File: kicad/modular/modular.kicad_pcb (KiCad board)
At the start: 2 copper layers, 50.5 x 78 mm, 53 parts, among them J1 CONN_PWR, J2 HEADER, J3 HEADER, U1 LM317, U2 LM337, U3 REF5010, U4 OPA4197

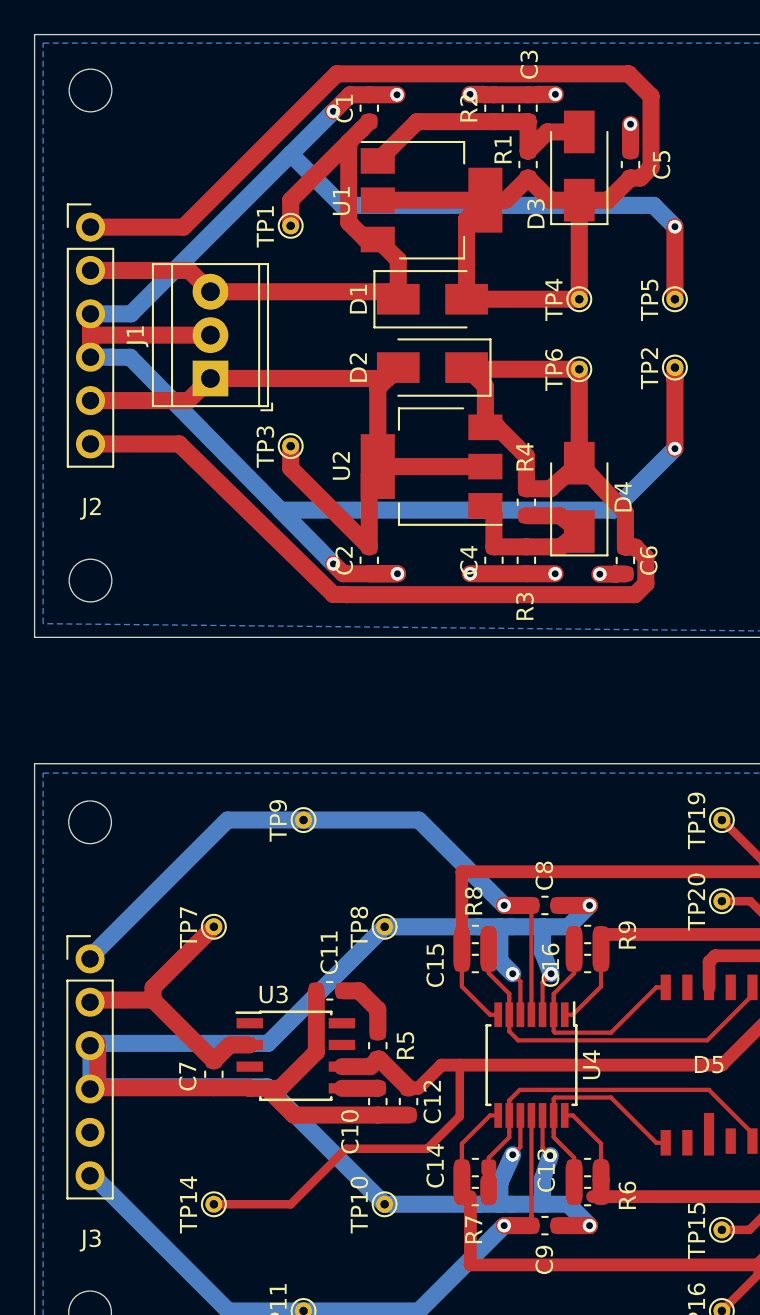
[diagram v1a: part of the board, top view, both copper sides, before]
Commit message: via stitched gnd trace of voltage reference, added zones around voltage regulators
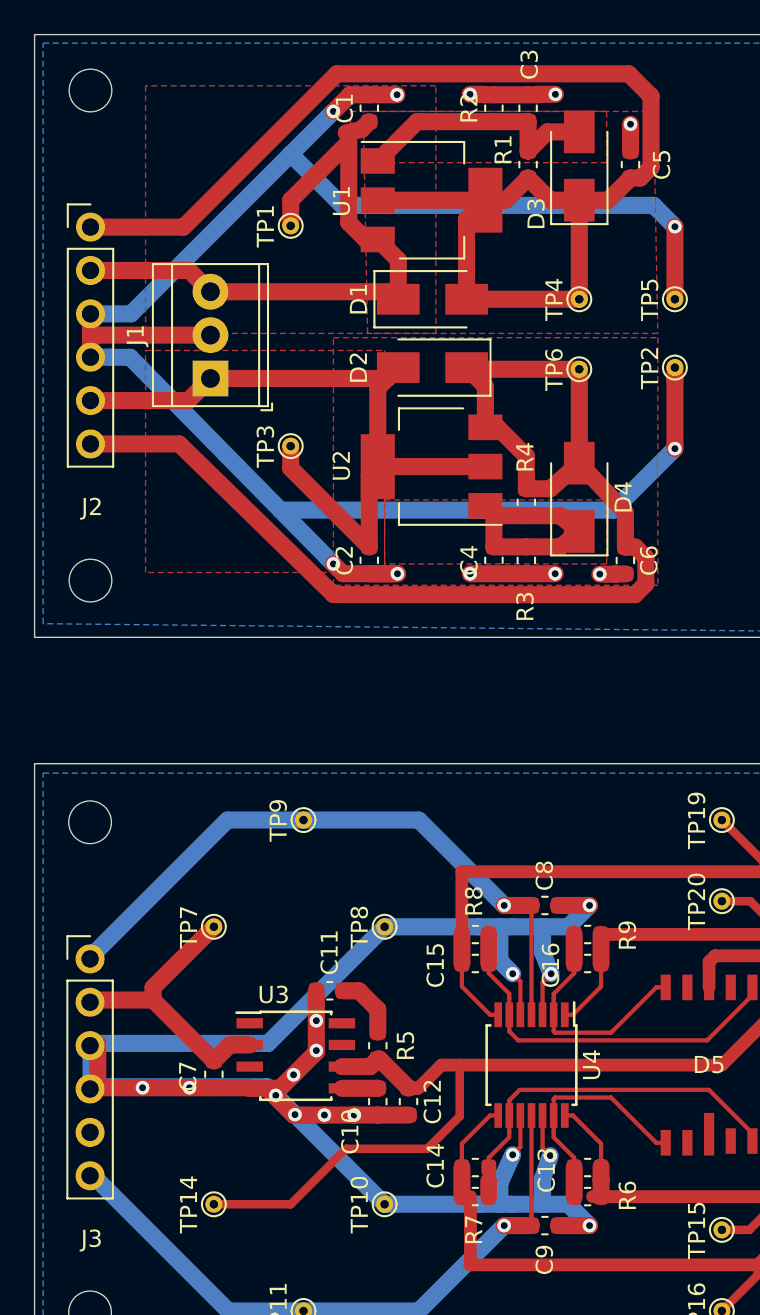
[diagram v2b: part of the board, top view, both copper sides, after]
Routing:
- net Net-(C4-Pad2): track 11.4 -> 14.0 mm
- net GND: vias 18 -> 27
- added copper zone on F.Cu, net +12V
- added copper zone on F.Cu, net +15V
- added copper zone on F.Cu, net -12V
- added copper zone on F.Cu, net -15V
- added copper zone on F.Cu, net Net-(C3-Pad1)
- added copper zone on F.Cu, net Net-(C4-Pad2)

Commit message: added pcb design of arithmetic board
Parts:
- added C17: 100n, Capacitor_SMD:C_0603_1608Metric, F.Cu at (205.7, 101.8)
- added C18: 100n, Capacitor_SMD:C_0603_1608Metric, F.Cu at (196.3, 98.5)
- added C19: 100n, Capacitor_SMD:C_0603_1608Metric, F.Cu at (193.4, 101.8)
- added C20: 100n, Capacitor_SMD:C_0603_1608Metric, F.Cu at (183.9, 98.5)
- added C21: ?, Capacitor_SMD:C_0603_1608Metric, F.Cu at (198.7, 94.4)
- added C22: ?, Capacitor_SMD:C_0603_1608Metric, F.Cu at (173.8, 94.5)
- added C23: ?, Capacitor_SMD:C_0603_1608Metric, F.Cu at (186.4, 94.4)
- added C24: 100n, Capacitor_SMD:C_0603_1608Metric, F.Cu at (180.7, 101.9)
- added C25: 100n, Capacitor_SMD:C_0603_1608Metric, F.Cu at (171.3, 98.6)
- added J4: Header, Connector_Header:PinHeader_2.54mm, F.Cu at (166.3, 97.5)
- added J5: DIFFX, Connector_Coaxial:SMA_Amphenol_132289_EdgeMount, F.Cu at (175.1, 88.9)
- added J6: DIFFY, Connector_Coaxial:SMA_Amphenol_132289_EdgeMount, F.Cu at (188.4, 88.9)
- added J7: SUM, Connector_Coaxial:SMA_Amphenol_132289_EdgeMount, F.Cu at (201.6, 88.9)
- added R10: 1k, Resistor_SMD:R_0603_1608Metric, F.Cu at (204.0, 104.8)
- added R11: 1k, Resistor_SMD:R_0603_1608Metric, F.Cu at (198.0, 104.8)
- added R12: 1k, Resistor_SMD:R_0603_1608Metric, F.Cu at (199.7, 104.8)
- added R13: 1k, Resistor_SMD:R_0603_1608Metric, F.Cu at (202.3, 104.8)
- added R14: 1k, Resistor_SMD:R_0603_1608Metric, F.Cu at (196.3, 101.8)
- added R15: 1k, Resistor_SMD:R_0603_1608Metric, F.Cu at (198.8, 96.1)
- added R16: 1k, Resistor_SMD:R_0603_1608Metric, F.Cu at (177.3, 104.8)
- added R17: 1k, Resistor_SMD:R_0603_1608Metric, F.Cu at (179.0, 104.8)
- added R18: 1k, Resistor_SMD:R_0603_1608Metric, F.Cu at (173.0, 104.8)
- added R19: 1k, Resistor_SMD:R_0603_1608Metric, F.Cu at (174.7, 104.8)
- added R20: 1k, Resistor_SMD:R_0603_1608Metric, F.Cu at (171.3, 101.9)
- added R21: 1k, Resistor_SMD:R_0603_1608Metric, F.Cu at (173.8, 96.2)
- added R22: 1k, Resistor_SMD:R_0603_1608Metric, F.Cu at (189.8, 104.8)
- added R23: 1k, Resistor_SMD:R_0603_1608Metric, F.Cu at (191.6, 104.8)
- added R24: 1k, Resistor_SMD:R_0603_1608Metric, F.Cu at (187.3, 104.8)
- added R25: 1k, Resistor_SMD:R_0603_1608Metric, F.Cu at (185.6, 104.8)
- added R26: 1k, Resistor_SMD:R_0603_1608Metric, F.Cu at (183.9, 101.8)
- added R27: 1k, Resistor_SMD:R_0603_1608Metric, F.Cu at (186.4, 96.1)
- added U5: OPA197, OPA197IDR:SOIC127P600X175-8N, F.Cu at (201.0, 100.1)
- added U7: OPA197, OPA197IDR:SOIC127P600X175-8N, F.Cu at (176.0, 100.2)
- added U8: OPA197, OPA197IDR:SOIC127P600X175-8N, F.Cu at (188.6, 100.1)
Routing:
- net /Arithmetic/X2: track 0.00 -> 66.9 mm, vias 0 -> 6
- net /Arithmetic/Y1: track 0.00 -> 56.7 mm, vias 0 -> 4
- net /Arithmetic/X1: track 0.00 -> 55.7 mm, vias 0 -> 4
- net /Arithmetic/Y2: track 0.00 -> 54.5 mm
- net Net-(C21-Pad2): track 0.00 -> 21.7 mm
- net Net-(C22-Pad2): track 0.00 -> 15.4 mm
- net Net-(C23-Pad2): track 0.00 -> 14.4 mm
- net /Arithmetic/SUM: track 0.00 -> 12.1 mm
- net Net-(R18-Pad1): track 0.00 -> 11.8 mm
- net Net-(R24-Pad1): track 0.00 -> 11.1 mm
- net /Arithmetic/DIFFY: track 0.00 -> 10.7 mm
- net /Arithmetic/DIFFX: track 0.00 -> 10.5 mm
- net GND: track 251.0 -> 261.4 mm, vias 27 -> 36
- net +12V: track 115.4 -> 122.7 mm
- net -12V: track 107.8 -> 114.7 mm
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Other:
- board size 50.5 x 78 mm -> 119.1 x 78 mm

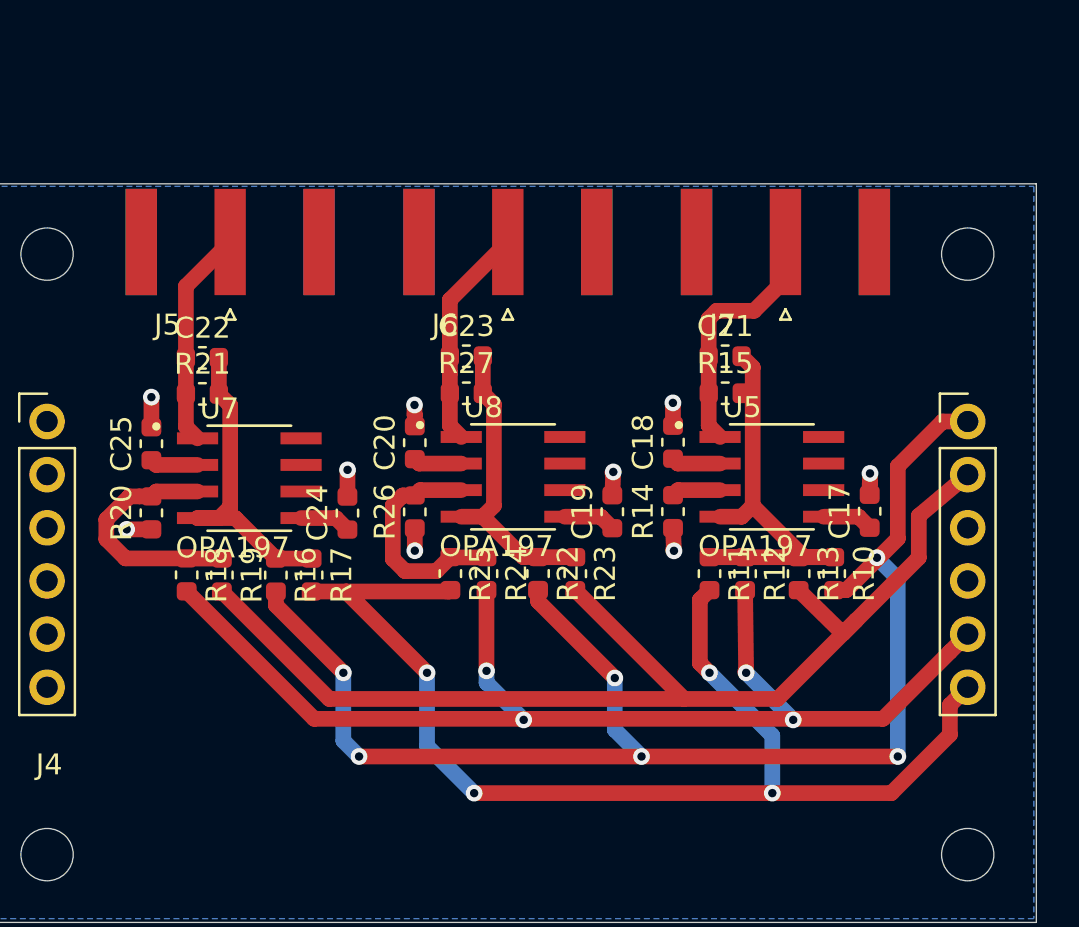
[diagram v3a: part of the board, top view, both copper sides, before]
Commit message: updated arithmetic schematic with resistor arrays and dual opamp, removed old footprints
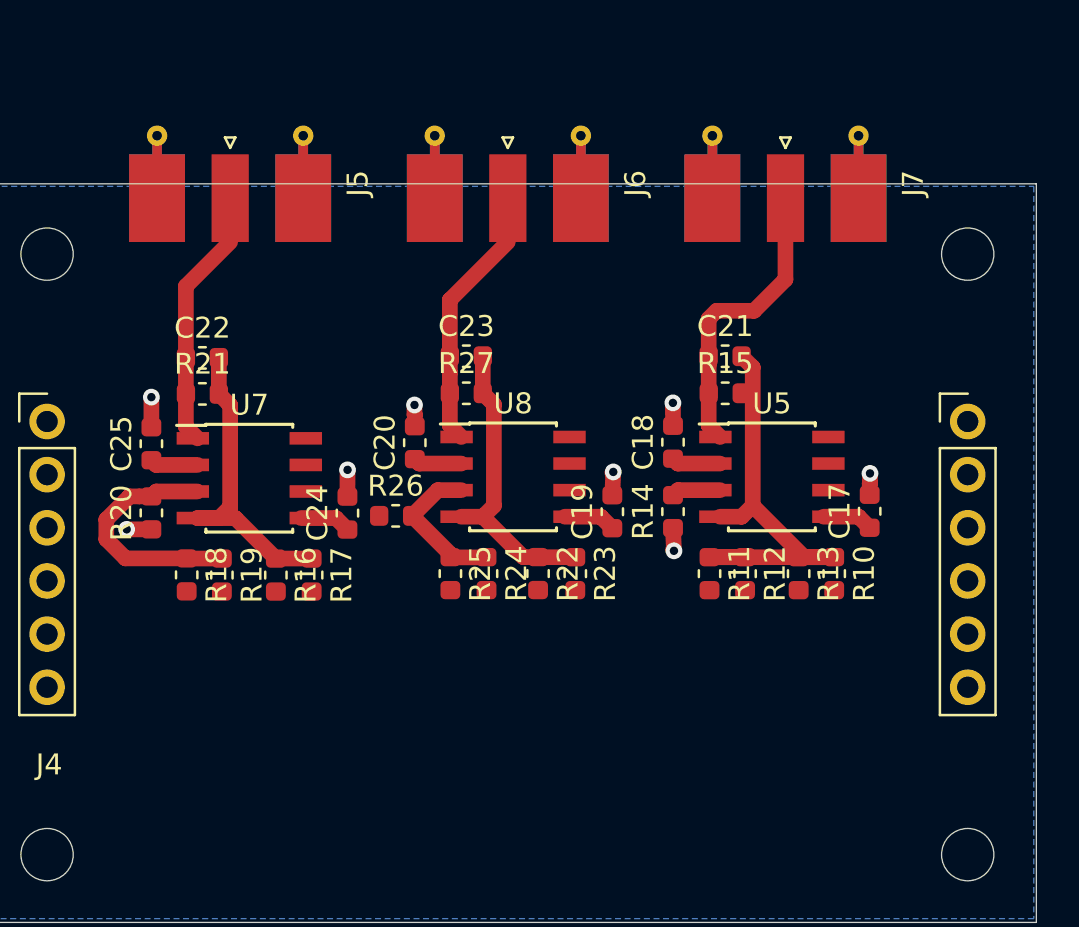
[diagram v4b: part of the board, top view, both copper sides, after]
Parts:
- J5, J6, J7: footprint Connector_Coaxial:SMA_Amphenol_132289_EdgeMount -> Connector_SMA:SMA_Molex_73251-2120_EdgeMount
- U5, U7, U8: footprint OPA197IDR:SOIC127P600X175-8N -> Package_SO:SOIC-8_3.9x4.9mm_P1.27mm
- moved R26 0.93 mm to (183.0, 102.0), turned to 0 degrees
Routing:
- net /Arithmetic/X2: track 66.9 -> 0.00 mm, vias 6 -> 0
- net /Arithmetic/Y1: track 56.7 -> 0.00 mm, vias 4 -> 0
- net /Arithmetic/X1: track 55.7 -> 0.00 mm, vias 4 -> 0
- net /Arithmetic/Y2: track 54.5 -> 0.00 mm
- net Net-(R24-Pad1): track 11.1 -> 7.32 mm
- net GND: track 261.4 -> 260.4 mm, vias 36 -> 35

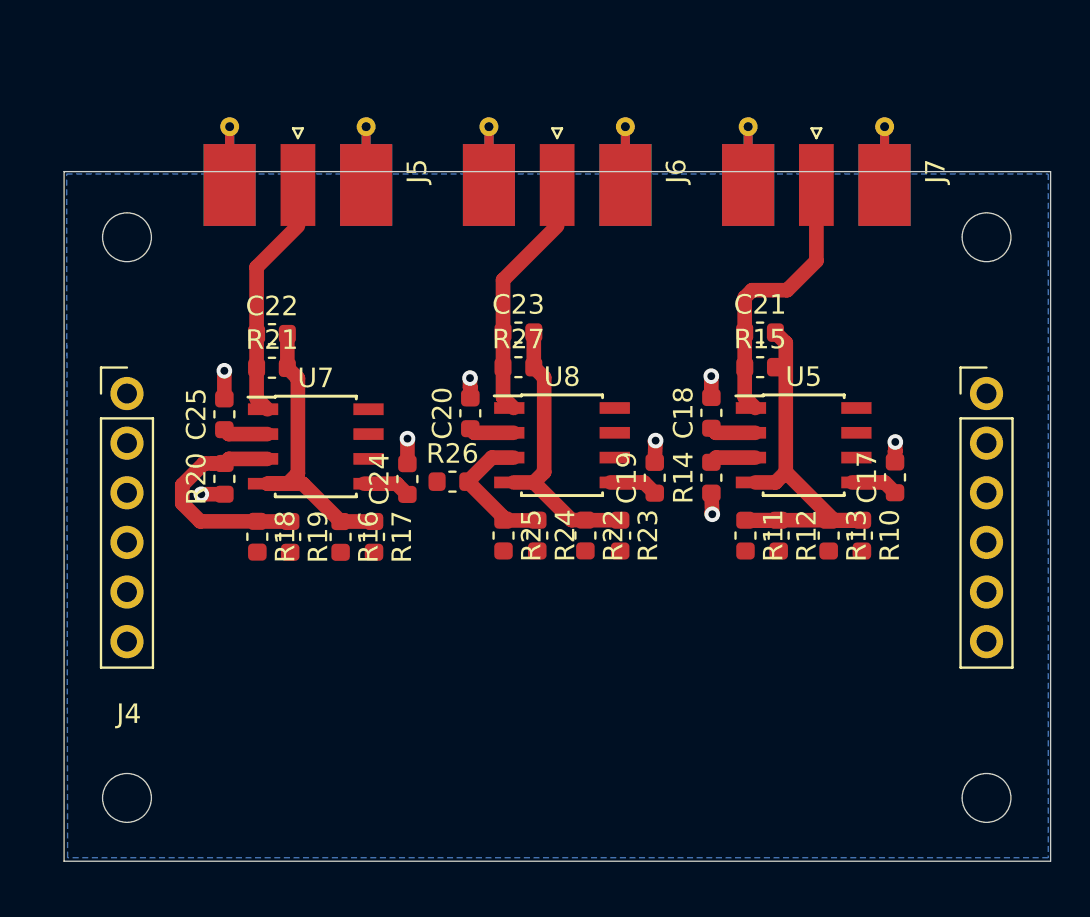
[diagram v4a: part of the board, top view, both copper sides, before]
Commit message: applied pcb design feedback to arithmetic board
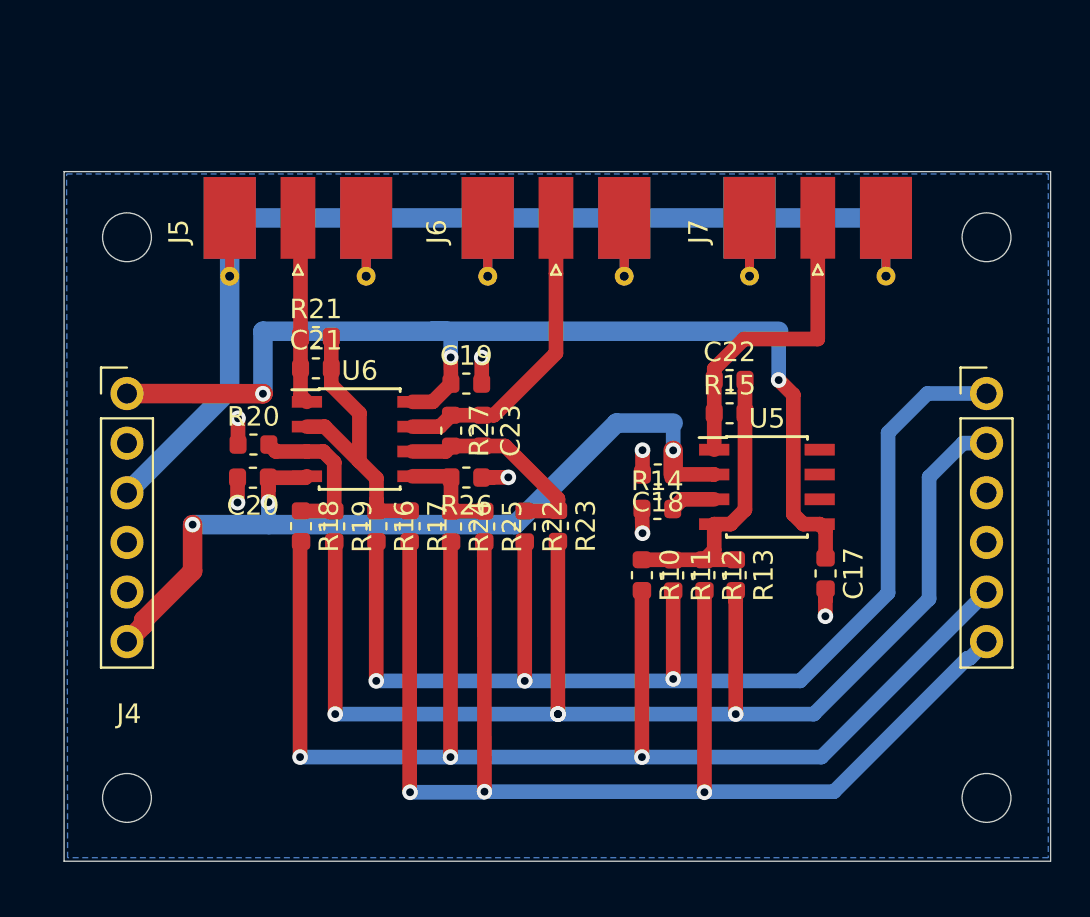
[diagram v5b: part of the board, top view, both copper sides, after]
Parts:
- removed C24, C25: 100n, Capacitor_SMD:C_0603_1608Metric
- removed U7, U8: OPA197, Package_SO:SOIC-8_3.9x4.9mm_P1.27mm
- added U6: OPA2197, Package_SO:SOIC-8_3.9x4.9mm_P1.27mm, F.Cu at (178.2, 99.8)
- C21, C22, C23: value ? -> 0
- moved C22 23.5 mm to (197.2, 96.8)
- moved C21 22.8 mm to (176.0, 96.2)
- moved C20 11.6 mm to (172.8, 101.8), turned to 180 degrees
- moved R10 11.4 mm to (192.7, 106.8)
- moved C19 10.8 mm to (183.7, 97.0), turned to 0 degrees
- moved C17 6.07 mm to (202.1, 106.7), turned to 270 degrees
- moved C23 5.34 mm to (184.6, 99.4), turned to 270 degrees
- moved R13 5.17 mm to (197.5, 106.8)
- moved R27 4.73 mm to (182.9, 99.4), turned to 270 degrees
- moved R24 4.44 mm to (182.9, 104.3)
- moved R12 4.31 mm to (195.9, 106.8)
- moved R11 4.22 mm to (194.3, 106.8)
- moved C18 4.18 mm to (193.5, 101.6), turned to 180 degrees
- moved R23 3.22 mm to (188.4, 104.3)
- moved R14 3.20 mm to (193.5, 103.4), turned to 0 degrees
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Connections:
- C21 pad 1: /Arithmetic/SUM -> /Arithmetic/DIFFX
- C22 pad 1: /Arithmetic/DIFFX -> /Arithmetic/SUM
- R10 pad 1: Net-(C21-Pad2) -> Net-(C22-Pad2)
- R10 pad 2: /Arithmetic/X2 -> /Arithmetic/X1
- R11 pad 1: Net-(C21-Pad2) -> Net-(C22-Pad2)
- R11 pad 2: /Arithmetic/Y1 -> /Arithmetic/X2
- R12 pad 1: Net-(C21-Pad2) -> Net-(C22-Pad2)
- R12 pad 2: /Arithmetic/X1 -> /Arithmetic/Y1
- R13 pad 1: Net-(C21-Pad2) -> Net-(C22-Pad2)
- R15 pad 2: Net-(C21-Pad2) -> Net-(C22-Pad2)
- R16 pad 1: Net-(C22-Pad2) -> Net-(C21-Pad2)
- R17 pad 1: Net-(C22-Pad2) -> Net-(C21-Pad2)
- R21 pad 2: Net-(C22-Pad2) -> Net-(C21-Pad2)
- U5 pad 4: Net-(C21-Pad2) -> Net-(C22-Pad2)
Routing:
- net /Arithmetic/X1: track 0.00 -> 69.1 mm, vias 0 -> 3
- net /Arithmetic/Y1: track 0.00 -> 68.7 mm, vias 0 -> 3
- net /Arithmetic/Y2: track 0.00 -> 67.3 mm, vias 0 -> 4
- net /Arithmetic/X2: track 0.00 -> 60.8 mm, vias 0 -> 3
- net GND: track 260.4 -> 310.1 mm, vias 35 -> 34
- net +12V: track 122.7 -> 170.9 mm, vias 1 -> 4
- net -12V: track 114.7 -> 151.1 mm, vias 1 -> 4
- net Net-(C21-Pad2): track 21.7 -> 15.4 mm
- net /Arithmetic/DIFFY: track 10.7 -> 15.8 mm
- net /Arithmetic/SUM: track 12.1 -> 16.3 mm
- net Net-(R18-Pad1): track 11.8 -> 7.92 mm
- net Net-(C23-Pad2): track 14.4 -> 11.0 mm
- net Net-(R24-Pad1): track 7.32 -> 5.42 mm
- net /Arithmetic/DIFFX: track 10.5 -> 9.61 mm
